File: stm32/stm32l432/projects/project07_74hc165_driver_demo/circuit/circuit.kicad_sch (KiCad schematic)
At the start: 2 parts, among them U1 STM32L432KCUx

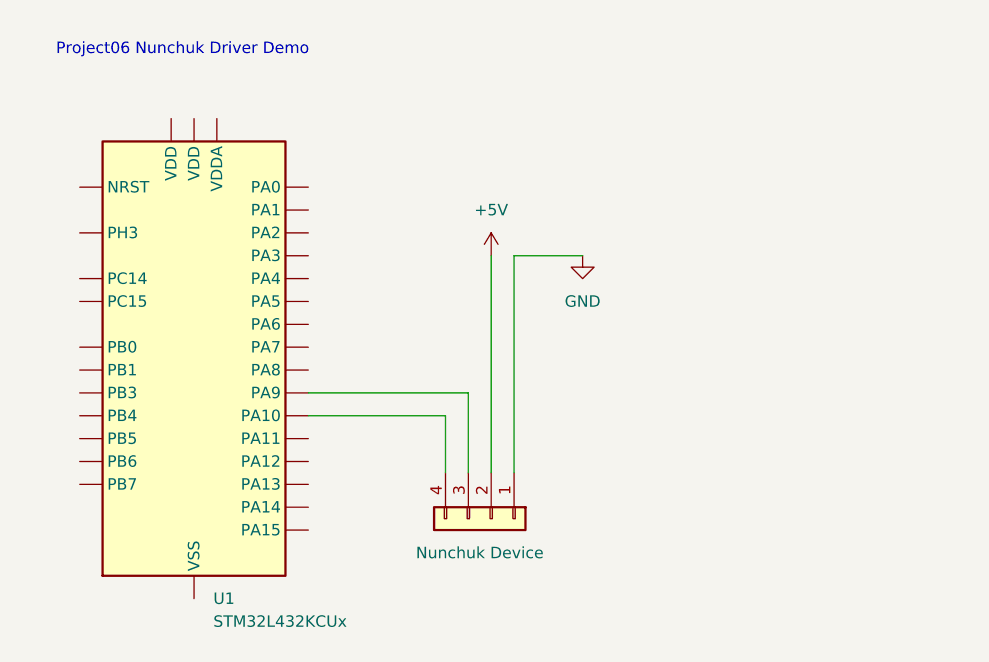
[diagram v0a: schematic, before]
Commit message: Updated kicad circuit diagram
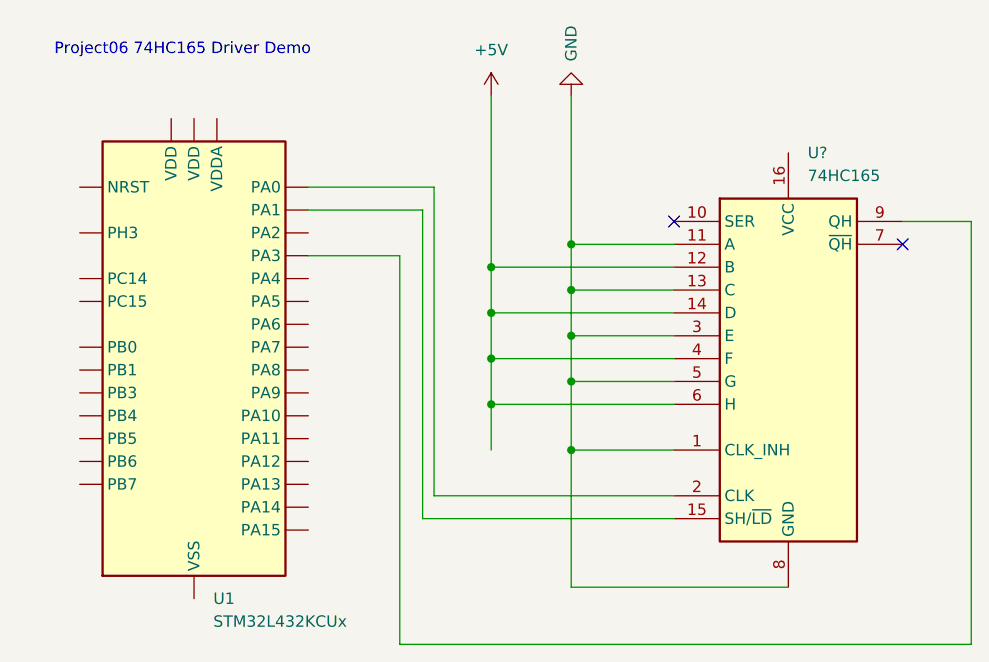
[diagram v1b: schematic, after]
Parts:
- removed J?: Nunchuk Device, symbol Connector_Generic:Conn_01x04
- added U?: 74HC165, symbol 74xx:74HC165
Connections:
- net +5V: now also U?.12 (B), U?.14 (D), U?.4 (F), U?.6 (H)
- net GND: now also U?.1 (CLK_INH), U?.11 (A), U?.13 (C), U?.3 (E), U?.5 (G), U?.8 (GND)
- net at U1.6 (PA0): now also U?.2 (CLK)
- net at U1.7 (PA1): now also U?.15 (SH/~{LD})
- net at U1.9 (PA3): now also U?.9 (QH)
- no-connect marks 0 -> 2
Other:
- note added: "Project06 74HC165 Driver Demo"
- note removed: "Project06 Nunchuk Driver Demo"
